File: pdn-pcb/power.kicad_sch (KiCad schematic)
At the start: 30 parts, among them J1 PH-2AW RHOS, Q2 FS8205A, SW3 On/Off Switch, U2 3.3v LDO, U2 TP4056, U3 DW01A, U4 MT3608

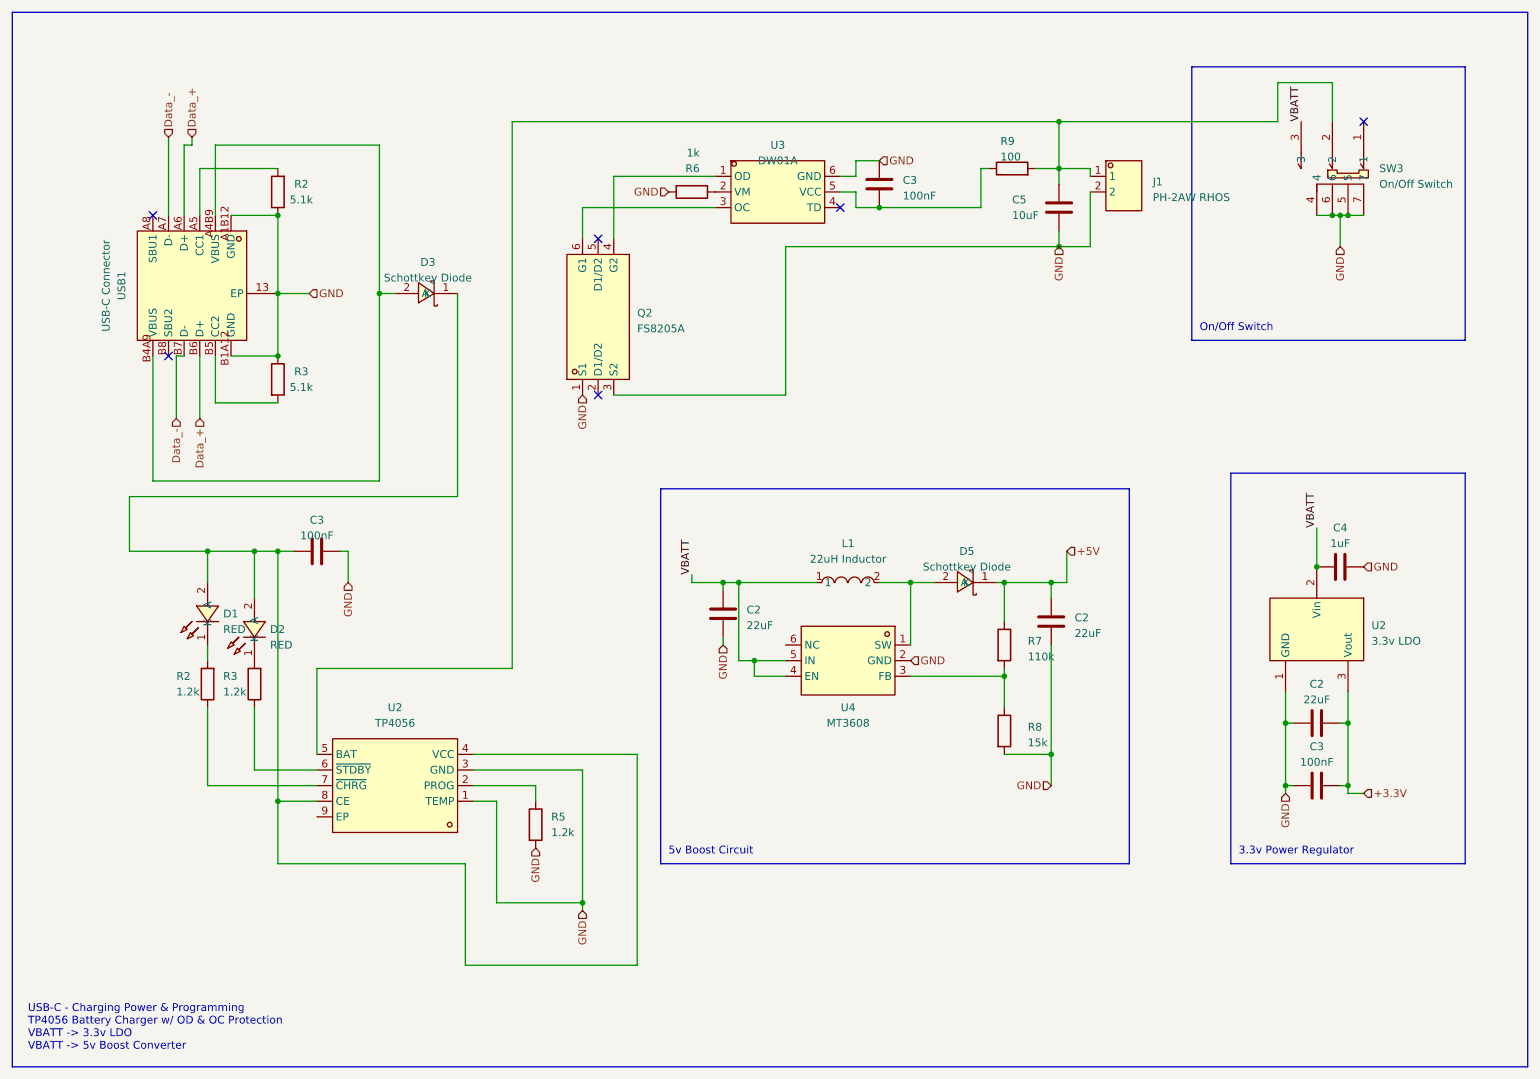
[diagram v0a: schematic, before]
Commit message: Updated 3v3 LDO to an LDL1117, reworked the brain board and added TVS protection.
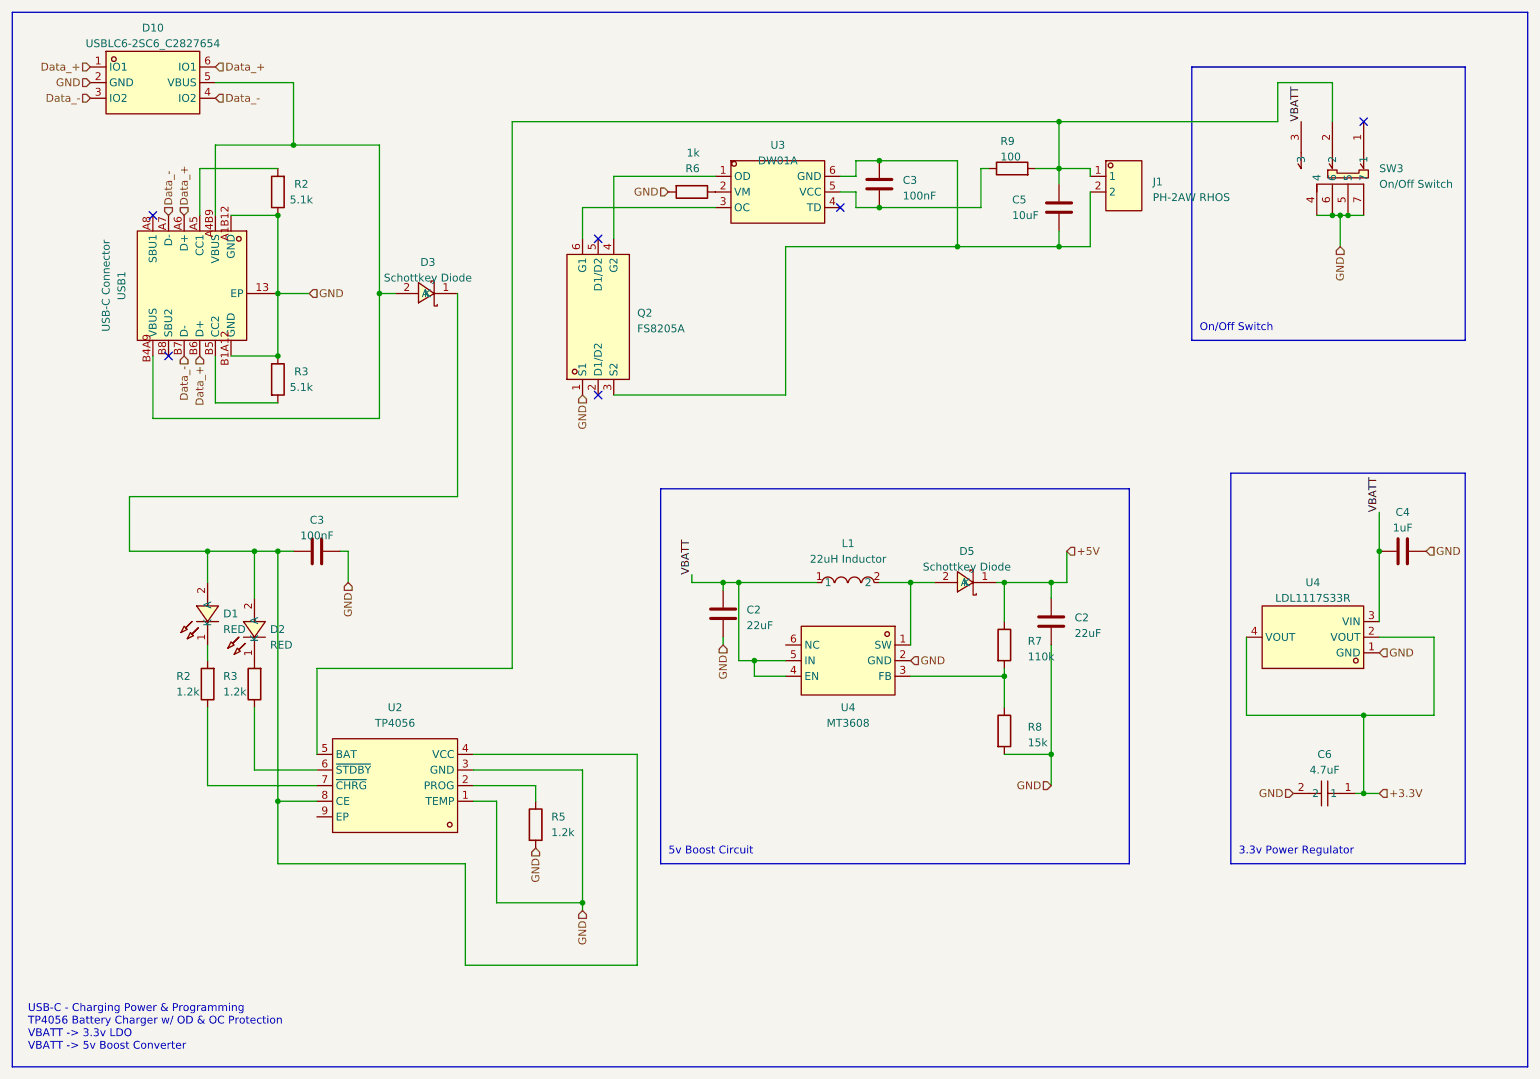
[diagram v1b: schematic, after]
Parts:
- removed C2: 22uF, Capacitor_SMD:C_1206_3216Metric, symbol Device:C
- removed C3: 100nF, global:C0402, symbol Device:C
- removed U2: 3.3v LDO, global:SOT-23-3_L2.9-W1.6-P1.90-LS2.8-BR, symbol pdn-internals:XC6206P332MR
- added C6: 4.7uF, global:C0805, symbol global:0805X475K160NT_C274245
- added D10: USBLC6-2SC6_C2827654, global:SOT-23-6_L2.9-W1.6-P0.95-LS2.8-BL, symbol global:USBLC6-2SC6_C2827654
- added U4: LDL1117S33R, global:SOT-223-4_L6.5-W3.5-P2.30-LS7.0-BR, symbol global:LDL1117S33R
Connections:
- net +3.3V: now also C6.1, U4.2 (VOUT), U4.4 (VOUT)
- net Data_+: now also D10.1 (IO1), D10.6 (IO1)
- net Data_-: now also D10.3 (IO2), D10.4 (IO2)
- net GND: now also C6.2, D10.2 (GND), U4.1 (GND); no longer C3.1, C5.2, J1.2, Q2.3 (S2), U3.6 (GND)
- net VBATT: now also U4.3 (VIN)
- net at D3.2 (A), USB1.A4B9 (VBUS), USB1.B4A9 (VBUS): now also D10.5 (VBUS)
- new net: C3.1, C5.2, J1.2, Q2.3 (S2), U3.6 (GND)
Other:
- moved on the sheet: C4

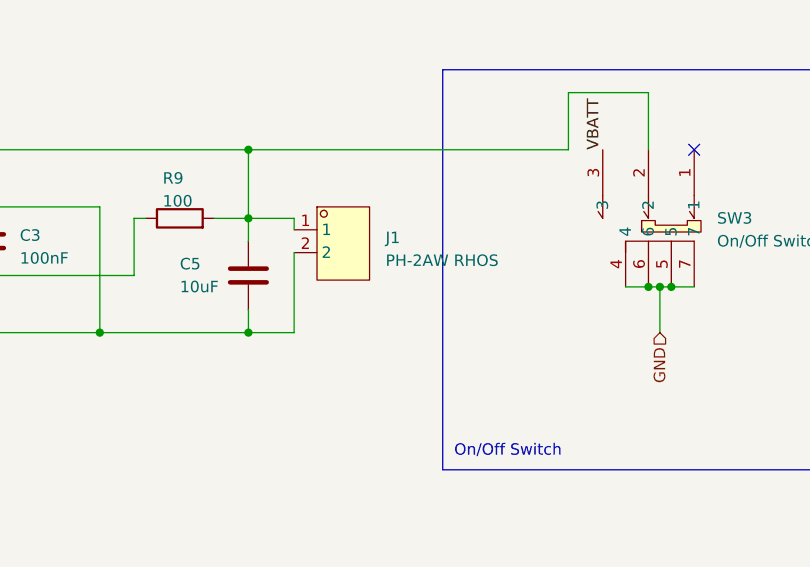
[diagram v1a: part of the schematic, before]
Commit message: Working Debug Menu.
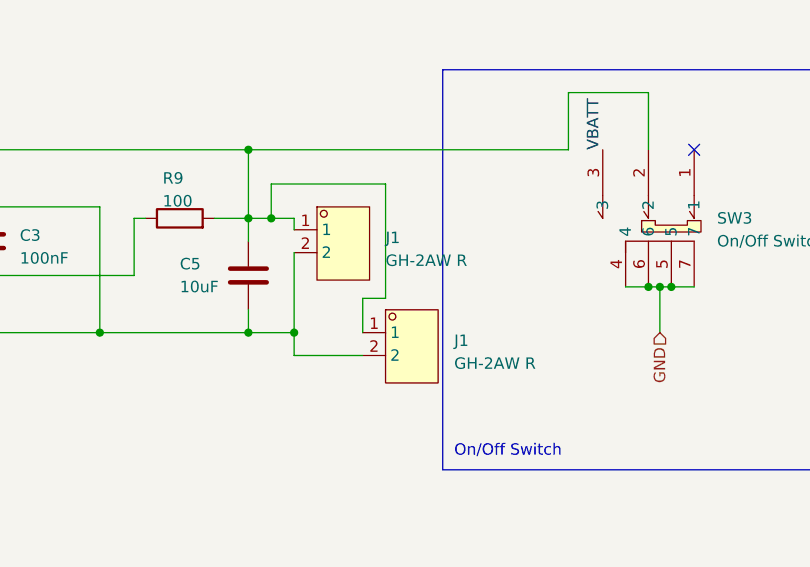
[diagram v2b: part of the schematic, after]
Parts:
- added J1: GH-2AW R, global:CONN-TH_GH 1x2P 1.25mm, symbol global:PH-2AWRHOS
- J1: value PH-2AW RHOS -> GH-2AW R; footprint global:CONN-TH_2P-P2.00_PH-2AW -> global:CONN-TH_GH 1x2P 1.25mm; LCSC Part C16965 -> C7433528
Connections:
- net at C5.1, J1.1, R9.2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: now also J1.1
- net at C3.1, C5.2, J1.2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: now also J1.2
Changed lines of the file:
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@@
   (junction (at 69.85 73.66) (diameter 0) (color 0 0 0 0)
   )
+  (junction (at 201.93 55.88) (diameter 0) (color 0 0 0 0)
+  )
   (junction (at 172.72 110.49) (diameter 0) (color 0 0 0 0)
   )
@@
   )
   (junction (at 196.85 43.18) (diameter 0) (color 0 0 0 0)
+  )
+  (junction (at 199.39 43.18) (diameter 0) (color 0 0 0 0)
   )
   (junction (at 167.64 49.53) (diameter 0) (color 0 0 0 0)
@@
     (stroke (width 0) (type default))
   )
+  (wire (pts (xy 212.09 39.37) (xy 212.09 52.07))
+    (stroke (width 0) (type default))
+  )
   (wire (pts (xy 186.69 110.49) (xy 187.96 110.49))
     (stroke (width 0) (type default))
@@
     (stroke (width 0) (type default))
   )
-  (wire (pts (xy 201.93 55.88) (xy 201.93 46.99))
+  (wire (pts (xy 201.93 46.99) (xy 201.93 55.88))
     (stroke (width 0) (type default))
   )
@@
     (stroke (width 0) (type default))
   )
+  (wire (pts (xy 212.09 52.07) (xy 209.55 52.07))
+    (stroke (width 0) (type default))
+  )
   (wire (pts (xy 161.29 46.99) (xy 163.83 46.99))
     (stroke (width 0) (type default))
@@
     (stroke (width 0) (type default))
   )
-  (wire (pts (xy 196.85 43.18) (xy 201.93 43.18))
+  (wire (pts (xy 199.39 43.18) (xy 201.93 43.18))
+    (stroke (width 0) (type default))
+  )
+  (wire (pts (xy 196.85 43.18) (xy 199.39 43.18))
     (stroke (width 0) (type default))
   )
@@
     (stroke (width 0) (type default))
   )
+  (wire (pts (xy 199.39 39.37) (xy 212.09 39.37))
+    (stroke (width 0) (type default))
+  )
+  (wire (pts (xy 199.39 43.18) (xy 199.39 39.37))
+    (stroke (width 0) (type default))
+  )
   (wire (pts (xy 72.39 39.37) (xy 86.36 39.37))
     (stroke (width 0) (type default))
@@
     (stroke (width 0) (type default))
   )
+  (wire (pts (xy 201.93 58.42) (xy 209.55 58.42))
+    (stroke (width 0) (type default))
+  )
   (wire (pts (xy 198.12 110.49) (xy 198.12 105.41))
     (stroke (width 0) (type default))
   )
+  (wire (pts (xy 201.93 55.88) (xy 201.93 58.42))
+    (stroke (width 0) (type default))
+  )
   (wire (pts (xy 58.42 120.65) (xy 58.42 123.19))
     (stroke (width 0) (type default))
@@
   )
   (wire (pts (xy 180.34 41.91) (xy 180.34 55.88))
+    (stroke (width 0) (type default))
+  )
+  (wire (pts (xy 209.55 52.07) (xy 209.55 55.88))
     (stroke (width 0) (type default))
   )
@@
       (effects (font (size 1.27 1.27)) (justify left))
     )
-    (property "Value" "PH-2AW RHOS" (at 212.09 47.88 0)
+    (property "Value" "GH-2AW R" (at 212.09 47.88 0)
       (effects (font (size 1.27 1.27)) (justify left))
     )
-    (property "Footprint" "global:CONN-TH_2P-P2.00_PH-2AW" (at 205.74 54.61 0)
-      (effects (font (size 1.27 1.27)) hide)
-    )
-    (property "Datasheet" "https://lcsc.com/product-detail/PH-Connectors_PH-2AW_C16965.html" (at 205.74 57.15 0)
-      (effects (font (size 1.27 1.27)) hide)
-    )
-    (property "LCSC Part" "C16965" (at 205.74 59.69 0)
+    (property "Footprint" "global:CONN-TH_GH 1x2P 1.25mm" (at 205.74 54.61 0)
+      (effects (font (size 1.27 1.27)) hide)
+    )
+    (property "Datasheet" "https://www.lcsc.com/datasheet/lcsc_datasheet_2306261512_Hong-Cheng-HCZZ0570-2_C7433528.pdf" (at 205.74 57.15 0)
+      (effects (font (size 1.27 1.27)) hide)
+    )
+    (property "LCSC Part" "C7433528" (at 205.74 59.69 0)
       (effects (font (size 1.27 1.27)) hide)
     )
@@
         )
       )
+    )
+  )
+  (symbol (lib_id "global:PH-2AWRHOS") (at 213.36 57.15 0) (unit 1)
+    (in_bom yes) (on_board yes) (dnp no) (fields_autoplaced)
+    (property "Reference" "J1" (at 219.71 56.77 0)
+      (effects (font (size 1.27 1.27)) (justify left))
+    )
+    (property "Value" "GH-2AW R" (at 219.71 59.31 0)
+      (effects (font (size 1.27 1.27)) (justify left))
+    )
+    (property "Footprint" "global:CONN-TH_GH 1x2P 1.25mm" (at 213.36 66.04 0)
+      (effects (font (size 1.27 1.27)) hide)
+    )
+    (property "Datasheet" "https://www.lcsc.com/datasheet/lcsc_datasheet_2306261512_Hong-Cheng-HCZZ0570-2_C7433528.pdf" (at 213.36 68.58 0)
+      (effects (font (size 1.27 1.27)) hide)
+    )
+    (property "LCSC Part" "C7433528" (at 213.36 71.12 0)
+      (effects (font (size 1.27 1.27)) hide)
+    )
+    (pin "1")
+    (pin "2")
+    (instances
+      (project "PDN"
+        (path "/df0bc267-025e-4c4e-a09b-51ff87d0c1db"
+          (reference "J1") (unit 1)
+        )
+        (path "/df0bc267-025e-4c4e-a09b-51ff87d0c1db/c306c3c8-b7c4-4bd2-bb28-1ed44c071e88"
+          (reference "J2") (unit 1)
+        )
+      )
